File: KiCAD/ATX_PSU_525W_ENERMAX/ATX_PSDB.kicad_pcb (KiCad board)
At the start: 2 copper layers, 160 x 170 mm, 91 parts, among them J1 Fan1, J10 ATX 12V1 Input, J11 Current Sens, J12 Molex: ATX 12V2 Input, J13 Molex: ATX 12V2 Input, J14 Molex: ATX 12V2 Input, J15 Potti, J16 Potti, J17 LED Yellow, J18 LED Yellow, J19 Volt Sens, J2 Power On Switch, J20 12V Out, J21 Volt Sens, J22 12V Out, J23 Molex: ATX 12V3 Input, J24 Current Sens, J25 Current Sens, J26 Molex: ATX 12V3 Input, J27 Molex: ATX 12V3 Input, J28 Fan1, J29 Fan1, J3 Standby LED, J30 Potti, J31 Potti, J32 LED Red, J33 LED Orange, J34 Volt Sens, J35 5V Out, J36 Volt Sens, J37 3.3V Out, J38 Terminal: +12V2 Input, J39 Terminal: +12V3 Input, J4 ATX 12V1 Input, J40 Current Sens, J41 Current Sens, J42 Terminal: +5V Input, J43 Terminal: +3.3V Input, J44 Terminal: Ground, J5 Potti, J6 LED Yellow, J7 Volt Sens, J8 12V Out, J9 Main ATX 24Pin, Q1 Q_NMOS_DGS, Q2 Q_NMOS_DGS, Q3 Q_NMOS_DGS, Q4 Q_NMOS_DGS, Q5 Q_NMOS_DGS, U1 ACS712xLCTR-20A, U2 ACS712xLCTR-20A, U3 ACS712xLCTR-20A, U4 ACS712xLCTR-20A, U5 ACS712xLCTR-20A

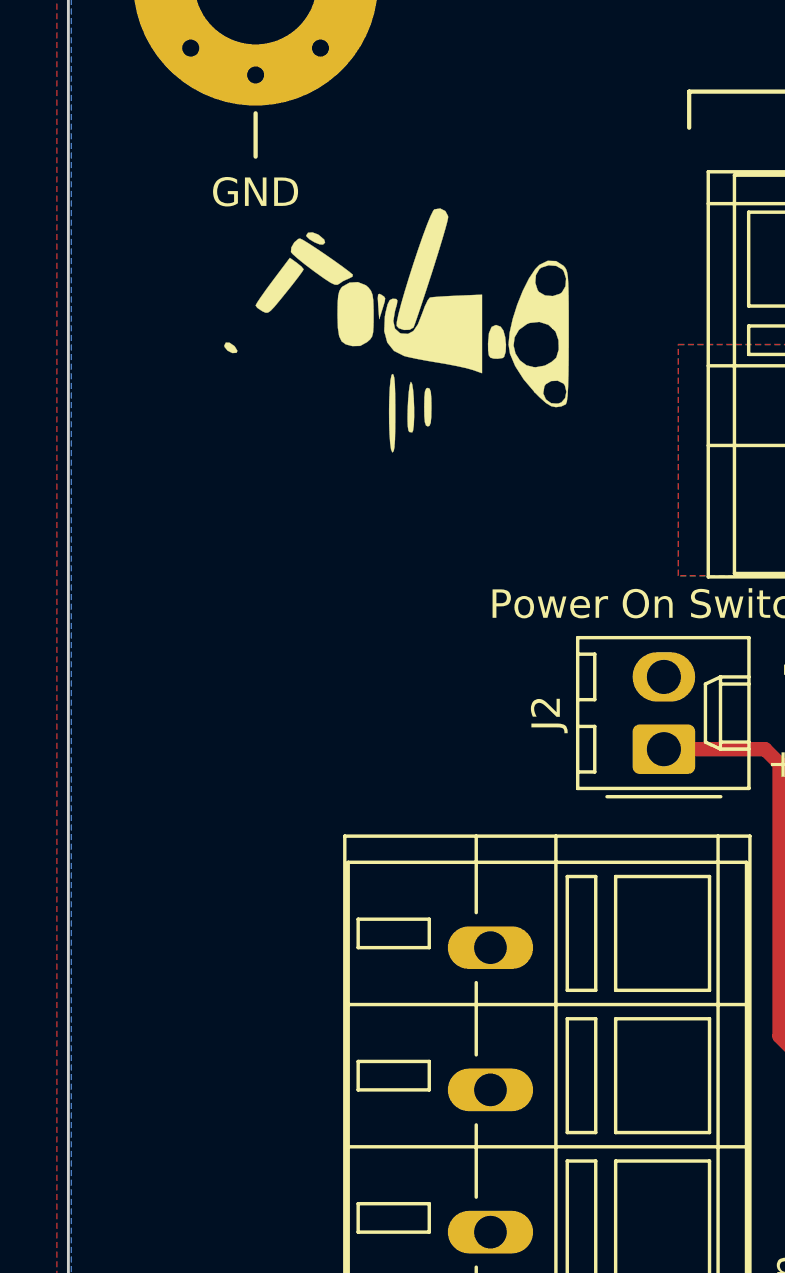
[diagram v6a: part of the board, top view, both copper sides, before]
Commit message: redesigned logo
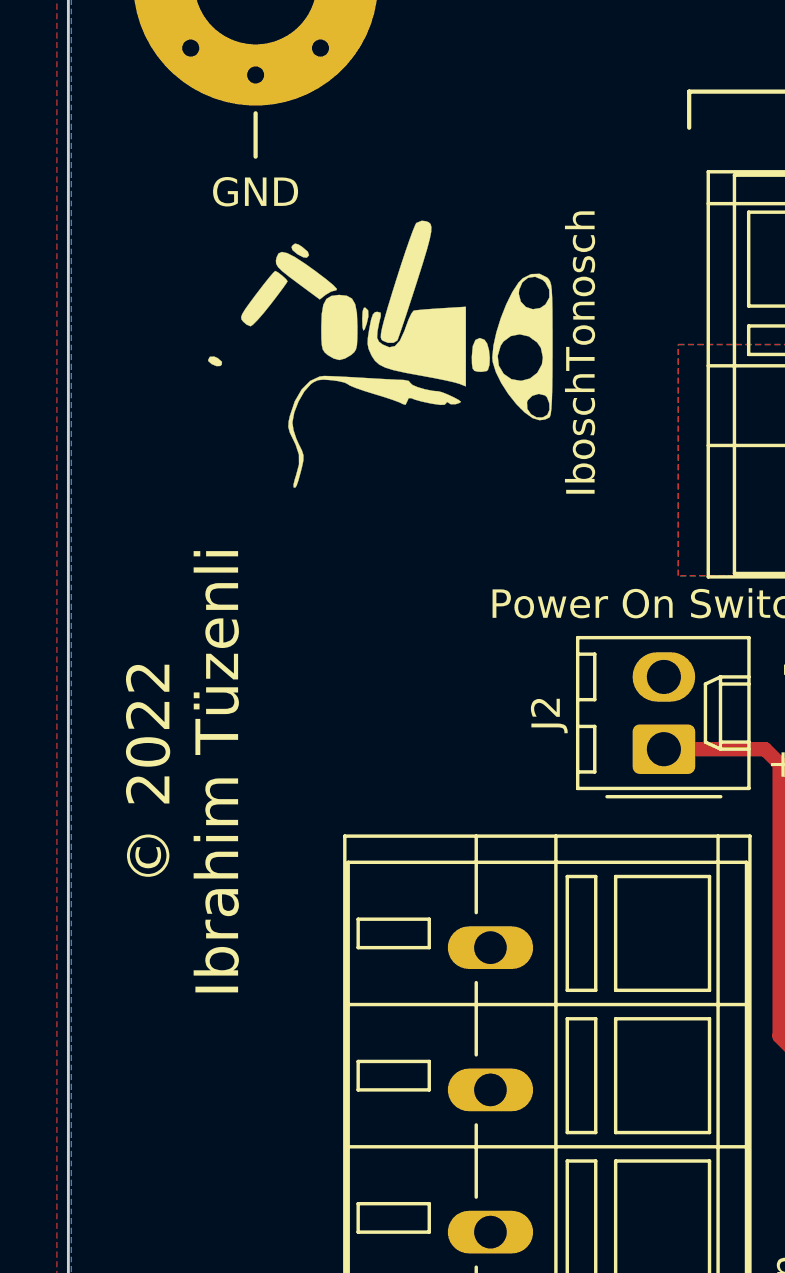
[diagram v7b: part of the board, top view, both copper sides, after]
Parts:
- moved G*** 0.73 mm to (26.6, 33.3)
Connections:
- C10 pad 2: +5V -> +F5V
- C2 pad 2: +5V -> +F5V
- C5 pad 2: +5V -> +F5V
- C6 pad 2: +5V -> +F5V
- C9 pad 2: +5V -> +F5V
- DZ4 pad 1: +5V -> +F5V
- F4 pad 2: +5V -> +F5V
- J11 pad 1: +5V -> +F5V
- J24 pad 1: +5V -> +F5V
- J25 pad 1: +5V -> +F5V
- J28 pad 1: +5V -> +F5V
- J40 pad 1: +5V -> +F5V
- J41 pad 1: +5V -> +F5V
- R10 pad 2: +5V -> +F5V
- R9 pad 1: +5V -> +F5V
- U1 pad 8: +5V -> +F5V
- U2 pad 8: +5V -> +F5V
- U3 pad 8: +5V -> +F5V
- U4 pad 1: +5V -> +F5V
- U4 pad 2: +5V -> +F5V
- U4 pad 8: +5V -> +F5V
- U5 pad 8: +5V -> +F5V
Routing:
- net +F5V: track 0.00 -> 165.9 mm, vias 0 -> 8
- net +5V: track 204.2 -> 38.3 mm, vias 8 -> 0
- added copper zone on B.Cu, net +F5V
- added copper zone on F.Cu, net +F5V

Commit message: correction
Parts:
- G***: value IboschTonosch -> IboshTonosh
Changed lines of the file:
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@@
       (effects (font (size 1.524 1.524) (thickness 0.3)))
     )
-    (fp_text value IboschTonosch (at -0.508 7.366 90) (layer F.SilkS)
+    (fp_text value IboshTonosh (at -0.508 7.366 90) (layer F.SilkS)
       (effects (font (size 1 1) (thickness 0.15)))
     )
